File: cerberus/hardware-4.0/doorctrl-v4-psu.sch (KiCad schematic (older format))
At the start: 30 parts, among them U2 MC34063, U3 L4960

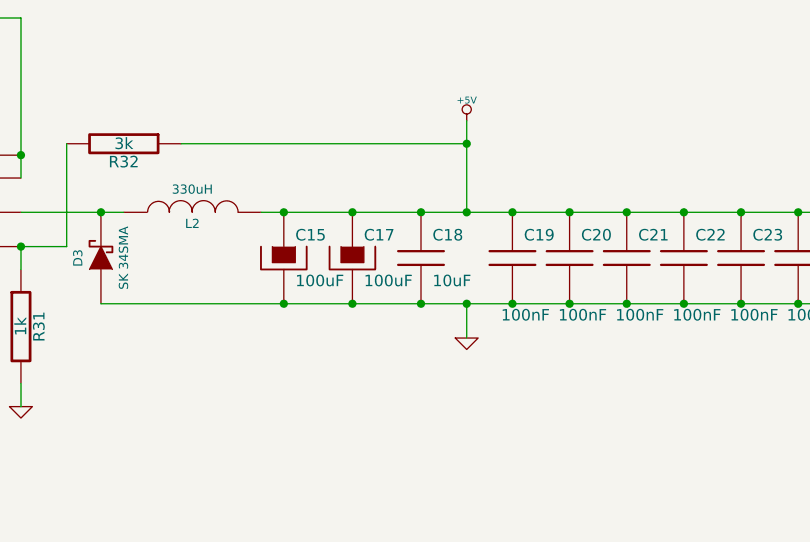
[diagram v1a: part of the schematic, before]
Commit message: Added torroid coil and proper diode packages
git-svn-id: file:///home/ff/projects/osaa/svn@222 a092026d-3e22-4cff-94a7-eaa6fdd35d37
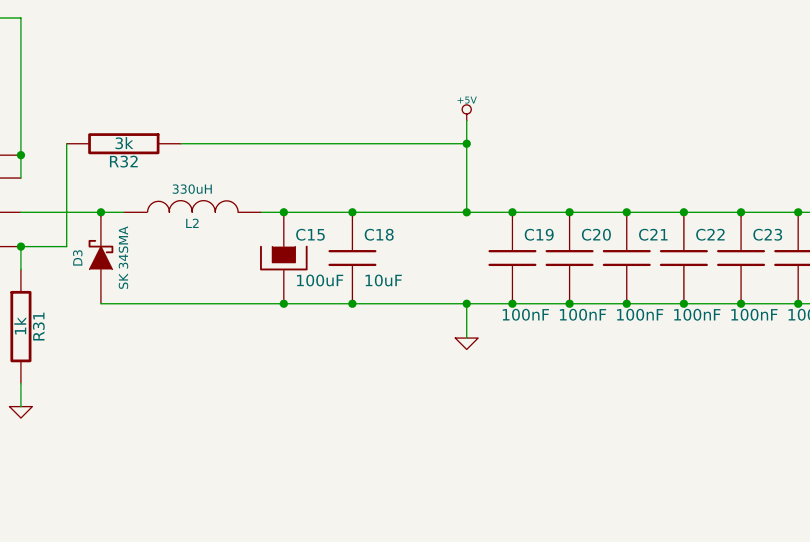
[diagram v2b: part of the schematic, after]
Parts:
- removed C17: 100uF, symbol CAPAPOL
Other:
- moved on the sheet: C18
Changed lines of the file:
@@
-EESchema Schematic File Version 2  date 2010-12-18T14:49:05 CET
+EESchema Schematic File Version 2  date 2010-12-19T21:45:09 CET
 LIBS:enc28j60
 LIBS:power
@@
 Sheet 6 6
 Title ""
-Date "18 dec 2010"
+Date "19 dec 2010"
 Rev ""
 Comp ""
@@
 $EndDescr
 $Comp
-L +5V #PWR43
+L +5V #PWR071
 U 1 1 4D0BB423
 P 5850 2200
-F 0 "#PWR43" H 5850 2290 20  0001 C CNN
+F 0 "#PWR071" H 5850 2290 20  0001 C CNN
 F 1 "+5V" H 5850 2290 30  0000 C CNN
 	1    5850 2200
@@
 Connection ~ 6550 3000
 Connection ~ 6050 3000
-Connection ~ 5350 3000
 Connection ~ 5850 2300
 Connection ~ 5050 2600
@@
 	4100 2750 4100 2300
 Connection ~ 5350 2600
-Connection ~ 5650 2600
 Connection ~ 5050 3000
-Connection ~ 5650 3000
+Connection ~ 5350 3000
 Connection ~ 6300 3000
 Connection ~ 7050 3000
@@
 $EndComp
 $Comp
-L GND #PWR42
+L GND #PWR072
 U 1 1 4D04D8EB
 P 5150 5250
-F 0 "#PWR42" H 5150 5250 30  0001 C CNN
+F 0 "#PWR072" H 5150 5250 30  0001 C CNN
 F 1 "GND" H 5150 5180 30  0001 C CNN
 	1    5150 5250
@@
 $EndComp
 $Comp
-L +12V #PWR41
+L +12V #PWR073
 U 1 1 4D04D8CC
 P 5150 4500
-F 0 "#PWR41" H 5150 4450 20  0001 C CNN
+F 0 "#PWR073" H 5150 4450 20  0001 C CNN
 F 1 "+12V" H 5150 4600 30  0000 C CNN
 	1    5150 4500
@@
 $EndComp
 $Comp
-L +24V #PWR37
+L +24V #PWR074
 U 1 1 4D04D7BB
 P 2200 4550
-F 0 "#PWR37" H 2200 4500 20  0001 C CNN
+F 0 "#PWR074" H 2200 4500 20  0001 C CNN
 F 1 "+24V" H 2200 4650 30  0000 C CNN
 	1    2200 4550
@@
 $EndComp
 $Comp
-L GND #PWR44
+L GND #PWR075
 U 1 1 4D04D42D
 P 5850 3150
-F 0 "#PWR44" H 5850 3150 30  0001 C CNN
+F 0 "#PWR075" H 5850 3150 30  0001 C CNN
 F 1 "GND" H 5850 3080 30  0001 C CNN
 	1    5850 3150
@@
 L C C18
 U 1 1 4D04D22A
-P 5650 2800
-F 0 "C18" H 5700 2900 50  0000 L CNN
-F 1 "10uF" H 5700 2700 50  0000 L CNN
-	1    5650 2800
-	1    0    0    -1
-$EndComp
-$Comp
-L CAPAPOL C17
-U 1 1 4D04D1BD
 P 5350 2800
-F 0 "C17" H 5400 2900 50  0000 L CNN
-F 1 "100uF" H 5400 2700 50  0000 L CNN
+F 0 "C18" H 5400 2900 50  0000 L CNN
+F 1 "10uF" H 5400 2700 50  0000 L CNN
 	1    5350 2800
 	1    0    0    -1
@@
 $EndComp
 $Comp
-L GND #PWR36
+L GND #PWR076
 U 1 1 4D04CF0D
 P 2200 3450
-F 0 "#PWR36" H 2200 3450 30  0001 C CNN
+F 0 "#PWR076" H 2200 3450 30  0001 C CNN
 F 1 "GND" H 2200 3380 30  0001 C CNN
 	1    2200 3450
@@
 $EndComp
 $Comp
-L GND #PWR40
+L GND #PWR077
 U 1 1 4D04CF06
 P 3900 3450
-F 0 "#PWR40" H 3900 3450 30  0001 C CNN
+F 0 "#PWR077" H 3900 3450 30  0001 C CNN
 F 1 "GND" H 3900 3380 30  0001 C CNN
 	1    3900 3450
@@
 $EndComp
 $Comp
-L GND #PWR39
+L GND #PWR078
 U 1 1 4D04CF02
 P 3050 3150
-F 0 "#PWR39" H 3050 3150 30  0001 C CNN
+F 0 "#PWR078" H 3050 3150 30  0001 C CNN
 F 1 "GND" H 3050 3080 30  0001 C CNN
 	1    3050 3150
@@
 $EndComp
 $Comp
-L +24V #PWR38
+L +24V #PWR079
 U 1 1 4D04CE42
 P 3050 1950
-F 0 "#PWR38" H 3050 1900 20  0001 C CNN
+F 0 "#PWR079" H 3050 1900 20  0001 C CNN
 F 1 "+24V" H 3050 2050 30  0000 C CNN
 	1    3050 1950

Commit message: Started laying out the PCB for real
git-svn-id: file:///home/ff/projects/osaa/svn@223 a092026d-3e22-4cff-94a7-eaa6fdd35d37
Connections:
- net +12V: now also R29.1; no longer R29.2, R30.1
- net at U3.2 (FBIN): now also R29.2, R30.1; no longer R29.1
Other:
- moved on the sheet: R29, R30
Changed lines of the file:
@@
-EESchema Schematic File Version 2  date 2010-12-19T21:45:09 CET
+EESchema Schematic File Version 2  date 2010-12-20T22:26:04 CET
 LIBS:enc28j60
 LIBS:power
@@
 LIBS:linear
 LIBS:atmel
+LIBS:diode
 LIBS:doorctrl-v4-cache
 EELAYER 24  0
@@
 Sheet 6 6
 Title ""
-Date "19 dec 2010"
+Date "20 dec 2010"
 Rev ""
 Comp ""
@@
 Comment4 ""
 $EndDescr
+Wire Wire Line
+	4950 4700 4950 5350
+Wire Wire Line
+	3550 5950 3550 6600
+Wire Wire Line
+	3550 5000 3550 5450
+Wire Wire Line
+	4950 2600 7550 2600
+Wire Wire Line
+	2350 4700 2200 4700
+Connection ~ 3300 6600
+Wire Wire Line
+	3300 5000 3300 6600
+Wire Wire Line
+	2550 5000 2550 5650
+Wire Wire Line
+	3050 5650 3050 5000
+Connection ~ 4950 4700
+Connection ~ 5000 5100
+Connection ~ 4800 5100
+Connection ~ 4800 4700
+Wire Wire Line
+	4650 4700 5150 4700
+Connection ~ 3900 4700
+Wire Wire Line
+	2800 6100 2800 6200
+Wire Wire Line
+	2300 6150 2300 6600
+Connection ~ 5850 2600
+Connection ~ 7300 2600
+Connection ~ 6800 2600
+Connection ~ 6300 2600
+Connection ~ 7550 3000
+Connection ~ 7050 3000
+Connection ~ 6300 3000
+Connection ~ 5350 3000
+Connection ~ 5050 3000
+Connection ~ 5350 2600
+Wire Wire Line
+	4100 2300 4100 2750
+Wire Wire Line
+	4100 2750 3900 2750
+Wire Wire Line
+	3050 3050 3050 3150
+Wire Wire Line
+	2200 2900 2200 2700
+Connection ~ 2200 2000
+Wire Wire Line
+	2400 2000 2200 2000
+Wire Wire Line
+	2200 1750 3900 1750
+Wire Wire Line
+	2200 1750 2200 2400
+Wire Wire Line
+	3050 2050 3050 1950
+Wire Wire Line
+	3900 1750 3900 2450
+Connection ~ 3900 2350
+Wire Wire Line
+	2900 2000 3050 2000
+Connection ~ 3050 2000
+Wire Wire Line
+	2200 3300 2200 3450
+Wire Wire Line
+	3900 3350 3900 3450
+Wire Wire Line
+	3900 2750 3900 2850
+Connection ~ 3900 2750
+Wire Wire Line
+	3900 2600 4350 2600
+Connection ~ 4250 2600
+Wire Wire Line
+	4600 2300 5850 2300
+Connection ~ 5050 2600
+Connection ~ 5850 2300
+Connection ~ 6050 3000
+Connection ~ 6550 3000
+Connection ~ 7300 3000
+Connection ~ 6800 3000
+Connection ~ 6050 2600
+Connection ~ 6550 2600
+Connection ~ 7050 2600
+Connection ~ 7550 2600
+Wire Wire Line
+	5850 3000 5850 3150
+Connection ~ 5850 3000
+Wire Wire Line
+	5850 2600 5850 2200
+Wire Wire Line
+	2550 5650 2300 5650
+Wire Wire Line
+	2550 6050 2550 6600
+Connection ~ 2550 6600
+Connection ~ 2800 6600
+Wire Wire Line
+	5150 4700 5150 4500
+Connection ~ 3900 5100
+Wire Wire Line
+	5150 5250 5150 5100
+Connection ~ 3550 6600
+Wire Wire Line
+	3050 6050 3050 6600
+Connection ~ 3050 6600
+Wire Wire Line
+	2800 5600 2800 5000
+Wire Wire Line
+	2300 6600 5000 6600
+Wire Wire Line
+	5000 6600 5000 5100
+Wire Wire Line
+	5150 5100 2200 5100
+Wire Wire Line
+	2200 4700 2200 4550
+Wire Wire Line
+	4050 4700 3750 4700
+Connection ~ 2550 5650
+Connection ~ 2200 4700
+Connection ~ 5150 4700
+Connection ~ 5150 5100
+Wire Wire Line
+	7550 3000 4250 3000
+Wire Wire Line
+	3550 5350 3650 5350
+Connection ~ 3550 5350
+Wire Wire Line
+	4950 5350 4150 5350
 $Comp
 L +5V #PWR071
@@
 	1    0    0    -1
 $EndComp
-Wire Wire Line
-	7550 3000 4250 3000
-Connection ~ 5150 5100
-Connection ~ 5150 4700
-Connection ~ 2200 4700
-Connection ~ 2550 5650
-Wire Wire Line
-	4050 4700 3750 4700
-Wire Wire Line
-	2200 4550 2200 4700
-Wire Wire Line
-	2200 5100 5150 5100
-Wire Wire Line
-	5000 5100 5000 6600
-Wire Wire Line
-	5000 6600 2300 6600
-Wire Wire Line
-	3550 5250 3550 5000
-Wire Wire Line
-	2800 5600 2800 5000
-Connection ~ 3050 6600
-Wire Wire Line
-	3050 6050 3050 6600
-Connection ~ 3550 6600
-Wire Wire Line
-	3550 6450 3550 6600
-Wire Wire Line
-	5150 5100 5150 5250
-Connection ~ 3900 5100
-Wire Wire Line
-	5150 4500 5150 4700
-Connection ~ 2800 6600
-Connection ~ 2550 6600
-Wire Wire Line
-	2550 6050 2550 6600
-Wire Wire Line
-	2300 5650 2550 5650
-Wire Wire Line
-	5850 2600 5850 2200
-Connection ~ 5850 3000
-Wire Wire Line
-	5850 3000 5850 3150
-Connection ~ 7550 2600
-Connection ~ 7050 2600
-Connection ~ 6550 2600
-Connection ~ 6050 2600
-Connection ~ 6800 3000
-Connection ~ 7300 3000
-Connection ~ 6550 3000
-Connection ~ 6050 3000
-Connection ~ 5850 2300
-Connection ~ 5050 2600
-Wire Wire Line
-	4600 2300 5850 2300
-Connection ~ 4250 2600
-Wire Wire Line
-	3900 2600 4350 2600
-Connection ~ 3900 2750
-Wire Wire Line
-	3900 2850 3900 2750
-Wire Wire Line
-	3900 3350 3900 3450
-Wire Wire Line
-	2200 3300 2200 3450
-Connection ~ 3050 2000
-Wire Wire Line
-	2900 2000 3050 2000
-Connection ~ 3900 2350
-Wire Wire Line
-	3900 2450 3900 1750
-Wire Wire Line
-	3050 2050 3050 1950
-Wire Wire Line
-	2200 2400 2200 1750
-Wire Wire Line
-	2200 1750 3900 1750
-Wire Wire Line
-	2400 2000 2200 2000
-Connection ~ 2200 2000
-Wire Wire Line
-	2200 2900 2200 2700
-Wire Wire Line
-	3050 3050 3050 3150
-Wire Wire Line
-	3900 2750 4100 2750
-Wire Wire Line
-	4100 2750 4100 2300
-Connection ~ 5350 2600
-Connection ~ 5050 3000
-Connection ~ 5350 3000
-Connection ~ 6300 3000
-Connection ~ 7050 3000
-Connection ~ 7550 3000
-Connection ~ 6300 2600
-Connection ~ 6800 2600
-Connection ~ 7300 2600
-Connection ~ 5850 2600
-Wire Wire Line
-	2300 6600 2300 6150
-Wire Wire Line
-	2800 6100 2800 6200
-Connection ~ 3900 4700
-Wire Wire Line
-	5150 4700 4650 4700
-Connection ~ 4800 4700
-Connection ~ 4800 5100
-Connection ~ 5000 5100
-Wire Wire Line
-	3550 5950 3550 5750
-Wire Wire Line
-	3550 5850 4950 5850
-Wire Wire Line
-	4950 5850 4950 4700
-Connection ~ 4950 4700
-Connection ~ 3550 5850
-Wire Wire Line
-	3050 5650 3050 5000
-Wire Wire Line
-	2550 5650 2550 5000
-Wire Wire Line
-	3300 5000 3300 6600
-Connection ~ 3300 6600
-Wire Wire Line
-	2200 4700 2350 4700
-Wire Wire Line
-	4950 2600 7550 2600
 $Comp
 L L4960 U3
@@
 L R R29
 U 1 1 4D04D9A5
-P 3550 5500
-F 0 "R29" V 3630 5500 50  0000 C CNN
-F 1 "6k2" V 3550 5500 50  0000 C CNN
-	1    3550 5500
-	1    0    0    -1
+P 3900 5350
+F 0 "R29" V 3980 5350 50  0000 C CNN
+F 1 "6k2" V 3900 5350 50  0000 C CNN
+	1    3900 5350
+	0    1    1    0
 $EndComp
 $Comp
 L R R30
 U 1 1 4D04D99F
-P 3550 6200
-F 0 "R30" V 3630 6200 50  0000 C CNN
-F 1 "4k7" V 3550 6200 50  0000 C CNN
-	1    3550 6200
+P 3550 5700
+F 0 "R30" V 3630 5700 50  0000 C CNN
+F 1 "4k7" V 3550 5700 50  0000 C CNN
+	1    3550 5700
 	1    0    0    -1
 $EndComp

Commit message: Finished the copper layers
git-svn-id: file:///home/ff/projects/osaa/svn@229 a092026d-3e22-4cff-94a7-eaa6fdd35d37
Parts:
- removed C21: 100nF, symbol C
- added C45, C46: 100nF, symbol C
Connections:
- net +5V: now also C45.1, C46.1
- net GND: now also C45.2, C46.2
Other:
- moved on the sheet: C22, C23, C24, C25
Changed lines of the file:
@@
-EESchema Schematic File Version 2  date 2010-12-21T17:47:20 CET
+EESchema Schematic File Version 2  date 2010-12-23T21:46:15 CET
 LIBS:enc28j60
 LIBS:power
@@
 LIBS:diode
 LIBS:doorctrl-v4-cache
-EELAYER 24  0
+EELAYER 25  0
 EELAYER END
 $Descr A4 11700 8267
 Sheet 6 6
 Title ""
-Date "21 dec 2010"
+Date "23 dec 2010"
 Rev ""
 Comp ""
@@
 $EndDescr
 Wire Wire Line
+	7800 2600 4950 2600
+Connection ~ 7550 3000
+Connection ~ 7550 2600
+Wire Wire Line
 	4950 4700 4950 5350
 Wire Wire Line
 	3550 5950 3550 6600
 Wire Wire Line
-	3550 5000 3550 5450
-Wire Wire Line
-	4950 2600 7550 2600
+	3550 5450 3550 5000
 Wire Wire Line
 	2350 4700 2200 4700
@@
 	2300 6150 2300 6600
 Connection ~ 5850 2600
-Connection ~ 7300 2600
-Connection ~ 6800 2600
+Connection ~ 7050 2600
+Connection ~ 6550 2600
 Connection ~ 6300 2600
-Connection ~ 7550 3000
-Connection ~ 7050 3000
+Connection ~ 7300 3000
+Connection ~ 6800 3000
 Connection ~ 6300 3000
 Connection ~ 5350 3000
@@
 	2200 1750 2200 2400
 Wire Wire Line
-	3050 2050 3050 1950
+	3050 1950 3050 2050
 Wire Wire Line
 	3900 1750 3900 2450
@@
 Connection ~ 3900 2750
 Wire Wire Line
-	3900 2600 4350 2600
+	4350 2600 3900 2600
 Connection ~ 4250 2600
 Wire Wire Line
@@
 Connection ~ 5850 2300
 Connection ~ 6050 3000
+Connection ~ 7050 3000
 Connection ~ 6550 3000
-Connection ~ 7300 3000
-Connection ~ 6800 3000
 Connection ~ 6050 2600
-Connection ~ 6550 2600
-Connection ~ 7050 2600
-Connection ~ 7550 2600
+Connection ~ 6800 2600
+Connection ~ 7300 2600
 Wire Wire Line
 	5850 3000 5850 3150
@@
 	2200 4700 2200 4550
 Wire Wire Line
-	4050 4700 3750 4700
+	3750 4700 4050 4700
 Connection ~ 2550 5650
 Connection ~ 2200 4700
@@
 Connection ~ 5150 5100
 Wire Wire Line
-	7550 3000 4250 3000
-Wire Wire Line
-	3550 5350 3650 5350
+	3650 5350 3550 5350
 Connection ~ 3550 5350
 Wire Wire Line
 	4950 5350 4150 5350
+Wire Wire Line
+	4250 3000 7800 3000
+$Comp
+L C C46
+U 1 1 4D139CE9
+P 7800 2800
+F 0 "C46" H 7850 2900 50  0000 L CNN
+F 1 "100nF" H 7750 2550 50  0000 L CNN
+	1    7800 2800
+	1    0    0    -1
+$EndComp
+$Comp
+L C C45
+U 1 1 4D139CE3
+P 7550 2800
+F 0 "C45" H 7600 2900 50  0000 L CNN
+F 1 "100nF" H 7500 2550 50  0000 L CNN
+	1    7550 2800
+	1    0    0    -1
+$EndComp
 $Comp
 L +5V #PWR071
@@
 L C C25
 U 1 1 4D04D39E
-P 7550 2800
-F 0 "C25" H 7600 2900 50  0000 L CNN
-F 1 "100nF" H 7500 2550 50  0000 L CNN
-	1    7550 2800
+P 7300 2800
+F 0 "C25" H 7350 2900 50  0000 L CNN
+F 1 "100nF" H 7250 2550 50  0000 L CNN
+	1    7300 2800
 	1    0    0    -1
 $EndComp
@@
 L C C24
 U 1 1 4D04D39B
-P 7300 2800
-F 0 "C24" H 7350 2900 50  0000 L CNN
-F 1 "100nF" H 7250 2550 50  0000 L CNN
-	1    7300 2800
+P 7050 2800
+F 0 "C24" H 7100 2900 50  0000 L CNN
+F 1 "100nF" H 7000 2550 50  0000 L CNN
+	1    7050 2800
 	1    0    0    -1
 $EndComp
@@
 L C C23
 U 1 1 4D04D398
-P 7050 2800
-F 0 "C23" H 7100 2900 50  0000 L CNN
-F 1 "100nF" H 7000 2550 50  0000 L CNN
-	1    7050 2800
+P 6800 2800
+F 0 "C23" H 6850 2900 50  0000 L CNN
+F 1 "100nF" H 6750 2550 50  0000 L CNN
+	1    6800 2800
 	1    0    0    -1
 $EndComp
@@
 L C C22
 U 1 1 4D04D394
-P 6800 2800
-F 0 "C22" H 6850 2900 50  0000 L CNN
-F 1 "100nF" H 6750 2550 50  0000 L CNN
-	1    6800 2800
-	1    0    0    -1
-$EndComp
-$Comp
-L C C21
-U 1 1 4D04D38F
 P 6550 2800
-F 0 "C21" H 6600 2900 50  0000 L CNN
+F 0 "C22" H 6600 2900 50  0000 L CNN
 F 1 "100nF" H 6500 2550 50  0000 L CNN
 	1    6550 2800
